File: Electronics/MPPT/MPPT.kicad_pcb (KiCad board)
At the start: 2 copper layers, 152.4 x 119.4 mm, 128 parts, among them J1 Solar Array, J2 Battery, J3 Car Power, J4 CAN_In, J5 CAN_Out, Q1 200N25N, Q2 200N25N, SW1 RESET, SW2 CAN Address, U1 PQMC3-D12-S9-S, U2 Nucleo_L432KC, U3 UCC37321, U4 INA210, U5 ADM3055E, U6 INA210, U7 CDSOT23-T24CAN

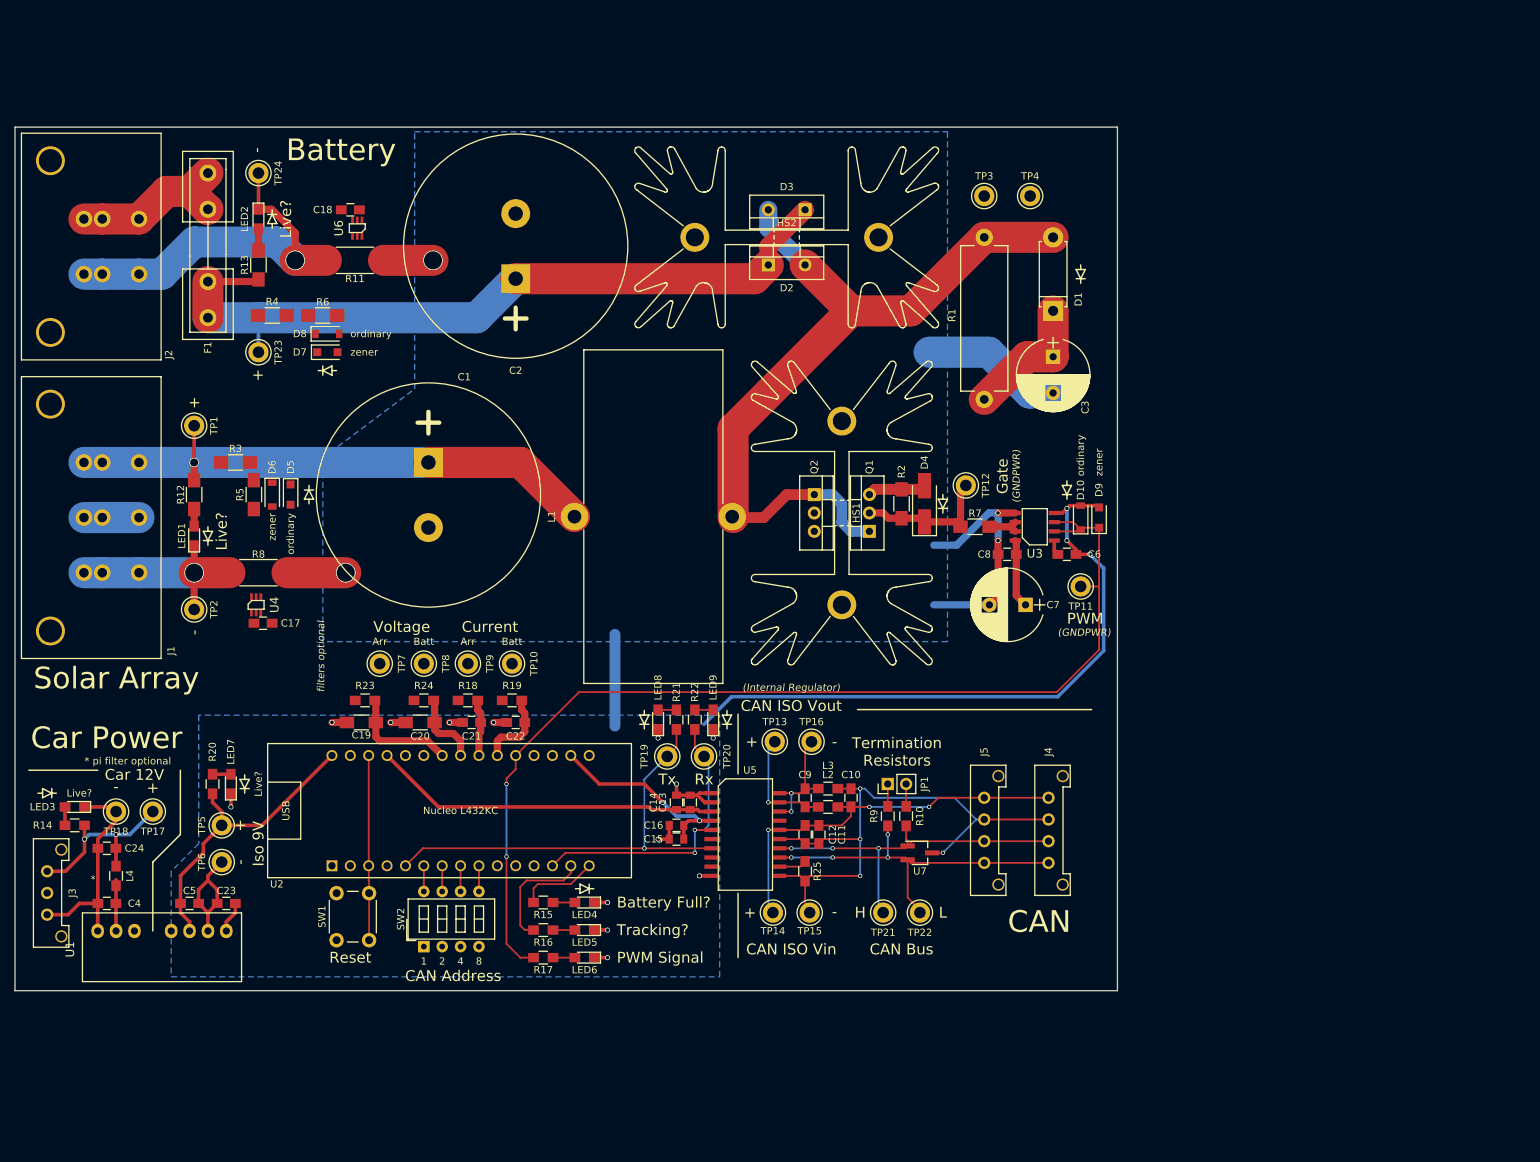
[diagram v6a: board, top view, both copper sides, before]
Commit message: MPPT: Finish wiring sensors
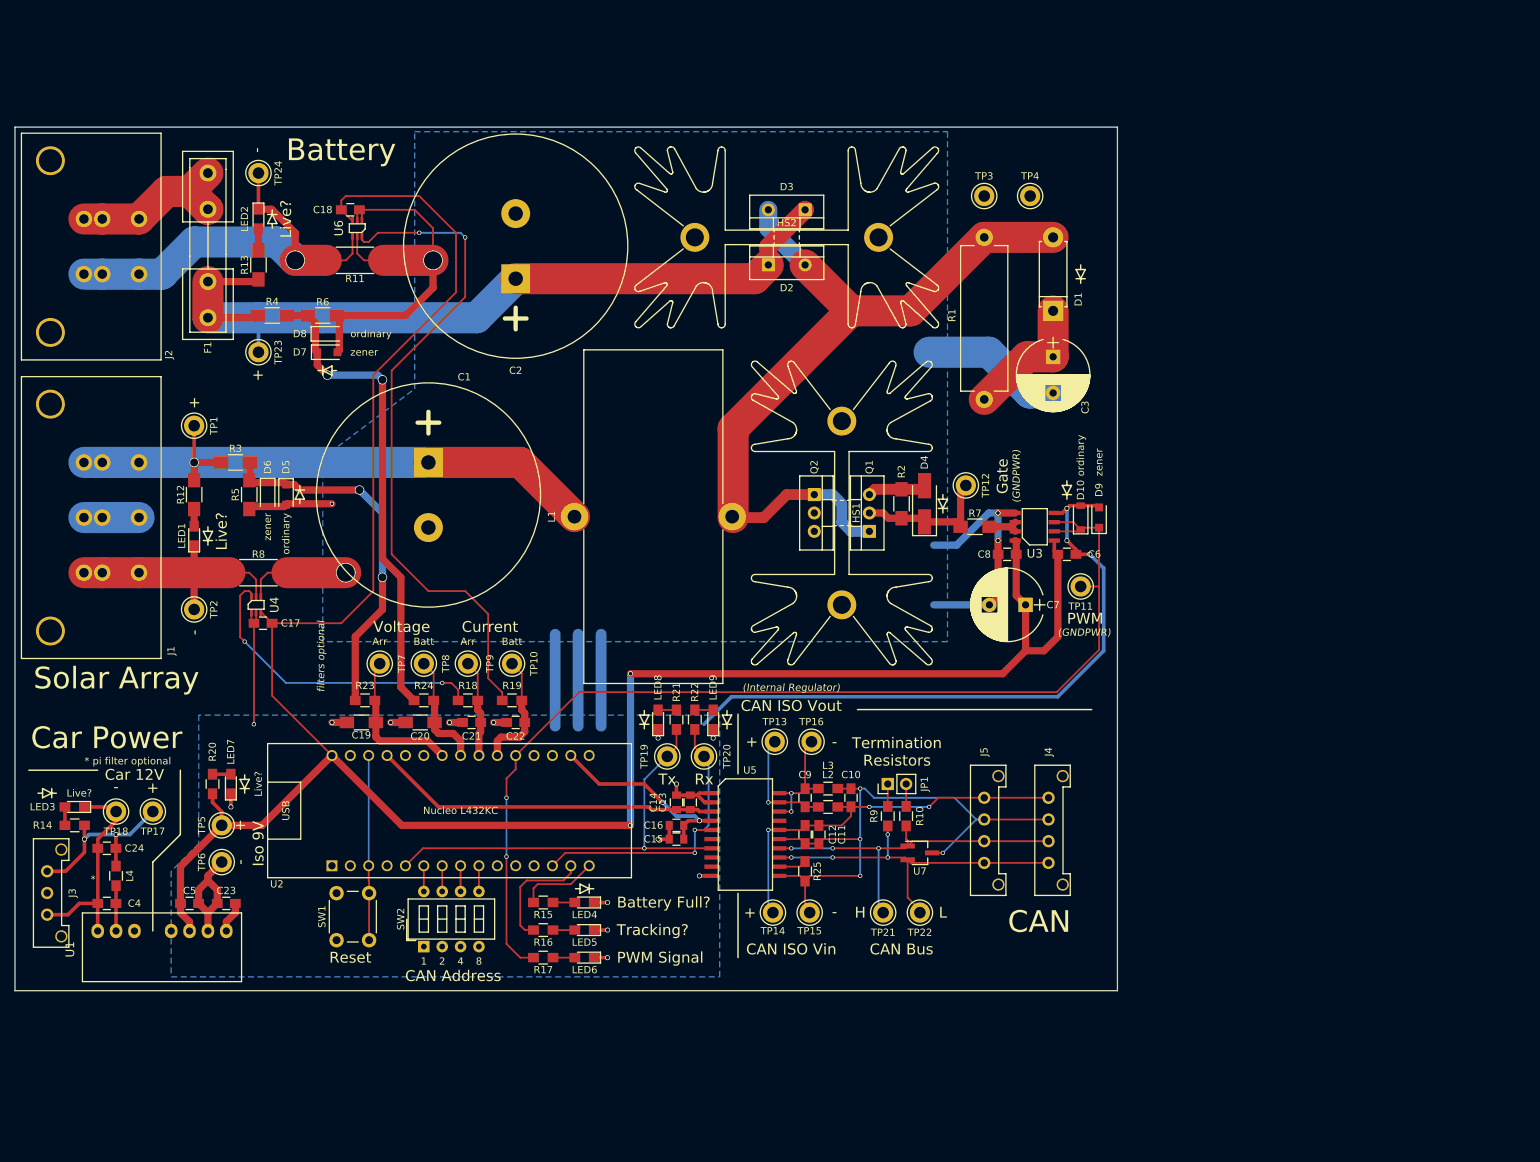
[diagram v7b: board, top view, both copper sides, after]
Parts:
- moved REF** 1.27 mm to (70.5, 81.9)
- moved D5 0.64 mm to (68.6, 81.9)
- moved R5 0.64 mm to (63.5, 81.9)
- moved D6 0.63 mm to (66.0, 81.9)
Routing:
- net +9VA: track 53.2 -> 314.0 mm, vias 0 -> 2
- net Net-(R19-Pad1): track 0.00 -> 93.2 mm, vias 0 -> 2
- net GNDPWR: track 213.3 -> 297.7 mm, vias 20 -> 22
- net Net-(D7-Pad1): track 0.00 -> 66.3 mm, vias 0 -> 2
- net Net-(D5-Pad1): track 0.00 -> 50.1 mm, vias 0 -> 2
- net Net-(R18-Pad1): track 0.00 -> 42.8 mm, vias 0 -> 2
- net (no net): track 12.7 -> 38.1 mm
- net /+Batt: track 107.7 -> 114.7 mm
- net /-Arr: track 30.3 -> 36.7 mm, vias 1 -> 0
- net /-Batt: track 51.6 -> 58.1 mm
- net /Battery_Voltage: track 10.4 -> 16.0 mm
- net /Battery_Current: track 10.8 -> 16.5 mm
- net /Array_Current: track 7.89 -> 13.5 mm
- net /Array_Voltage: track 15.3 -> 20.7 mm
- net /+Arr: track 78.4 -> 82.2 mm

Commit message: MPPT: Set GND plane parameters; fix some wires so KiCad shuts up.
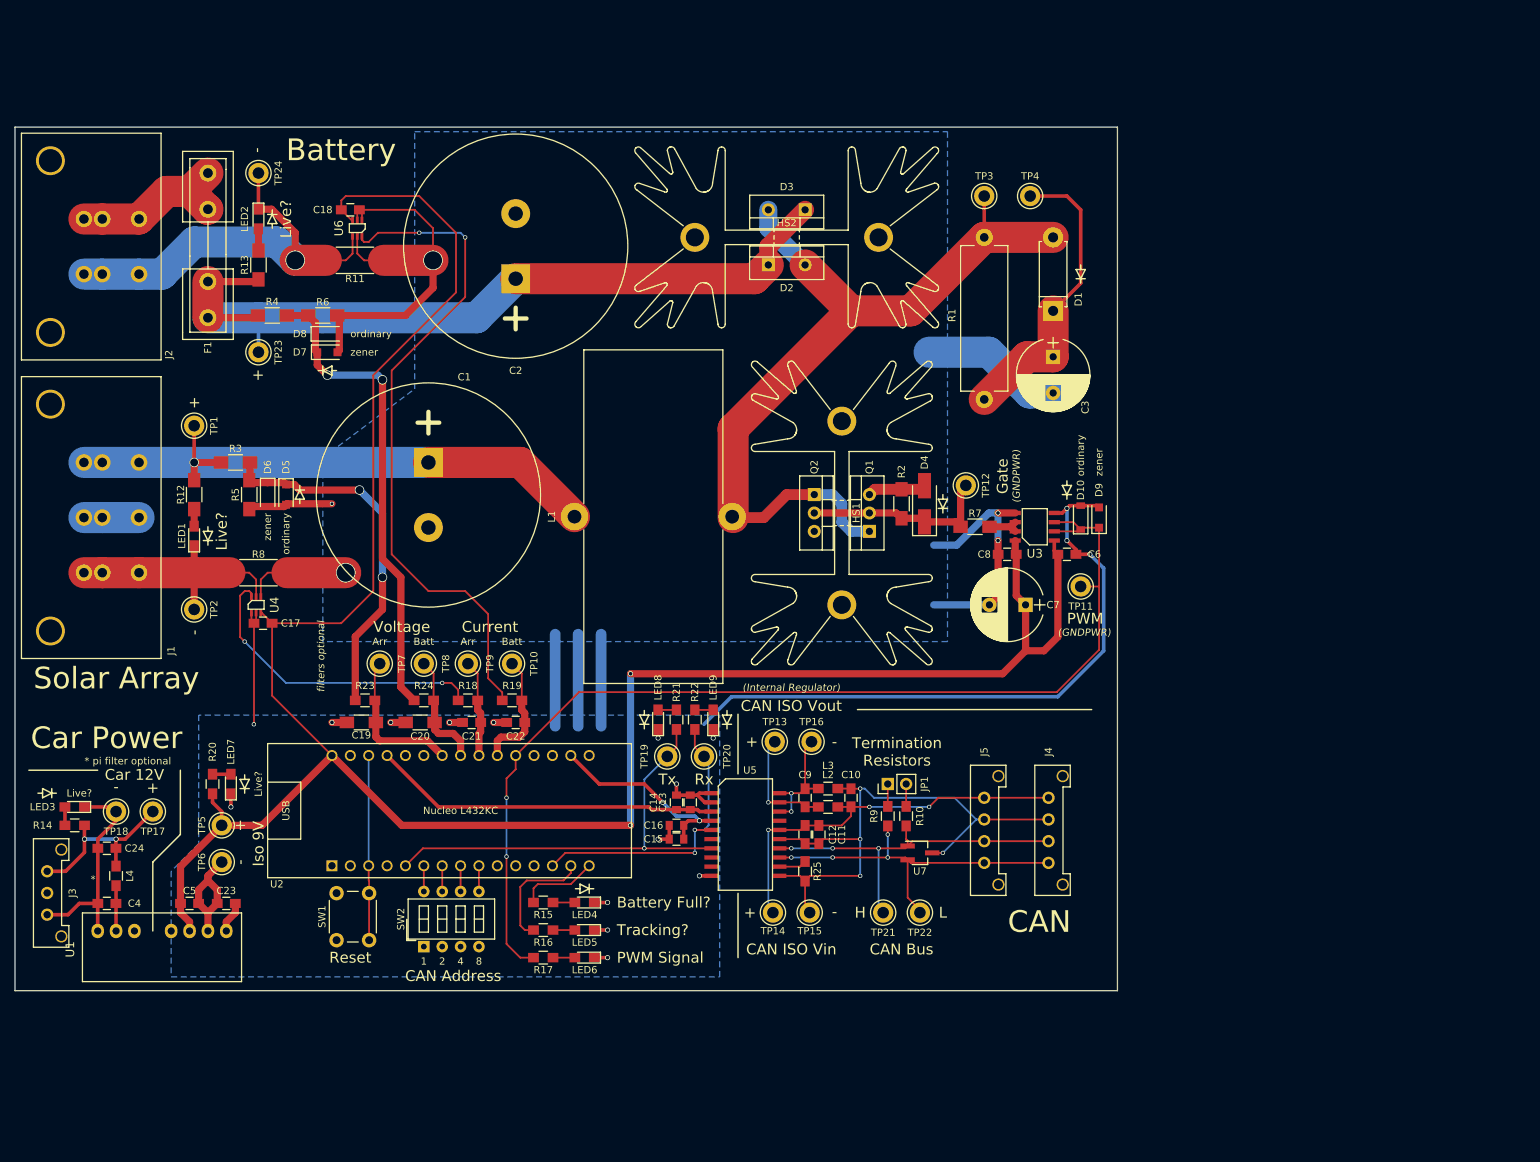
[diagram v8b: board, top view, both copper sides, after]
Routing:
- net Net-(C3-Pad1): track 18.3 -> 41.6 mm
- net /Drive_PWM: track 19.5 -> 27.1 mm
- net Net-(D1-Pad2): track 109.9 -> 115.6 mm
- net /-Arr: track 36.7 -> 35.4 mm
- net +12V: track 25.4 -> 24.8 mm
